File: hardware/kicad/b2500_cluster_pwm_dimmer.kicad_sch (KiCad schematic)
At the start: 35 parts, among them J1 Phoenix MKDS-1,5-5-5.08, Q1 FQP27P06, Q2 2N7000, SW1 CAL, U1 XIAO RP2040, U2 Pololu D36V28F5

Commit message: Add KiCad PCB layout (placed + poured, signal nets for GUI routing)
Generate b2500_cluster_pwm_dimmer.kicad_pcb via hardware/scripts/gen_pcb.py
(pcbnew API). Per the chosen workflow, the board is delivered placed and
ground-poured with the high-current connector nets pre-routed; the remaining
signal nets are left as ratsnest for interactive routing in the KiCad GUI.

- Signal-flow floorplan on a 94x62 mm 2-layer board, fitted against real
  footprint courtyards: connector left, input protection across the top,
  buck + 5V path top-right, DIM sense divider mid-board (kept away from the
  MOSFET switching node), MCU centre, gate drive + Q1 bottom-left by the
  output pin. Zero courtyard/edge violations.
- GND pours on both layers + stitching vias; M3 mounting holes tied to GND.
- VIN_RAW (on B.Cu) and PWM_OUT pre-routed wide with hand-authored,
  pad-avoiding waypoints. DRC clean except the deliberate signal ratsnest.
- Per-pin connector silk, USB power warning, cluster-illumination-only note,
  and all seven required test points.
- Refactor the netlist into hardware/scripts/netlist.py as the single source
  of truth shared by the schematic and board generators. Q2 -> wider-pitch
  TO-92 footprint for hand soldering and clearance.
- Top-view render committed for reference (hardware/kicad/pcb_top.png).

Co-Authored-By: Claude Fable 5 <noreply@anthropic.com>
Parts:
- Q2: footprint Package_TO_SOT_THT:TO-92_Inline -> Package_TO_SOT_THT:TO-92_Inline_Wide
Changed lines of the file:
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@@
     (property "Reference" "Q2" (at 76.2 217.14 0) (effects (font (size 1.27 1.27))))
     (property "Value" "2N7000" (at 76.2 245.14 0) (effects (font (size 1.27 1.27))))
-    (property "Footprint" "Package_TO_SOT_THT:TO-92_Inline" (at 76.2 231.14 0) (effects (font (size 1.27 1.27)) hide))
+    (property "Footprint" "Package_TO_SOT_THT:TO-92_Inline_Wide" (at 76.2 231.14 0) (effects (font (size 1.27 1.27)) hide))
     (property "Datasheet" "" (at 76.2 231.14 0) (effects (font (size 1.27 1.27)) hide))
     (property "Description" "" (at 76.2 231.14 0) (effects (font (size 1.27 1.27)) hide))

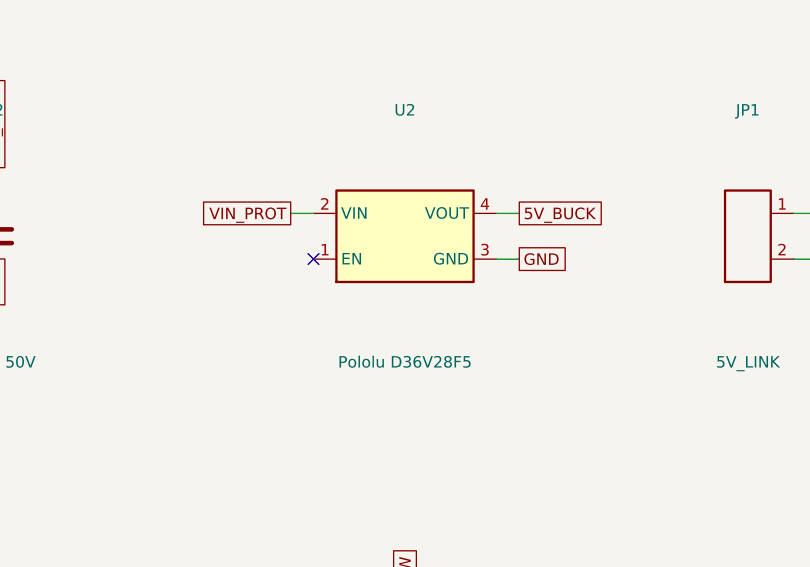
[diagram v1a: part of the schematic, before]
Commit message: Fix U2 buck land: off-board 3-pin wired header (audit finding)
A datasheet/footprint audit found the U2 land was wrong: the custom Pololu
D36V28F5 footprint had 4 pads in an unverified order, but the real module has
6 connections (offset PG plus two GNDs) and Pololu does not publish the edge
pin order in text. A mis-built buck could put 12 V on the 5 V rail.

Replace it with an orientation-proof connection: U2 is now a labeled 3-pin
header (VIN / GND / VOUT 5V) for the module mounted off-board and wired
label-to-label. EN (default-on) and PG are unused.

- netlist.py: U2 -> PinHeader_1x03, pads VIN/GND/VOUT -> VIN_PROT/GND/5V_BUCK.
- gen_sch.py: buck symbol reduced to 3 pins (VIN/GND/VOUT). ERC clean.
- gen_pcb.py: re-place U2, add per-pin silk and OFF-BOARD BUCK label, fix the
  VIN_PROT and 5V_BUCK routing pad refs. Fully routed, DRC 0/0.
- Delete the incorrect Pololu_D36V28F5.kicad_mod; refresh gerbers, BOM, docs.

Audit also verified (correct, no change): XIAO RP2040 footprint pinout plus
0.6in/0.1in spacing, FQP27P06 G-D-S, 2N7000 S-G-D, BAT54S pin-3 common, and
diode (cathode = pad 1) polarities.

Co-Authored-By: Claude Fable 5 <noreply@anthropic.com>
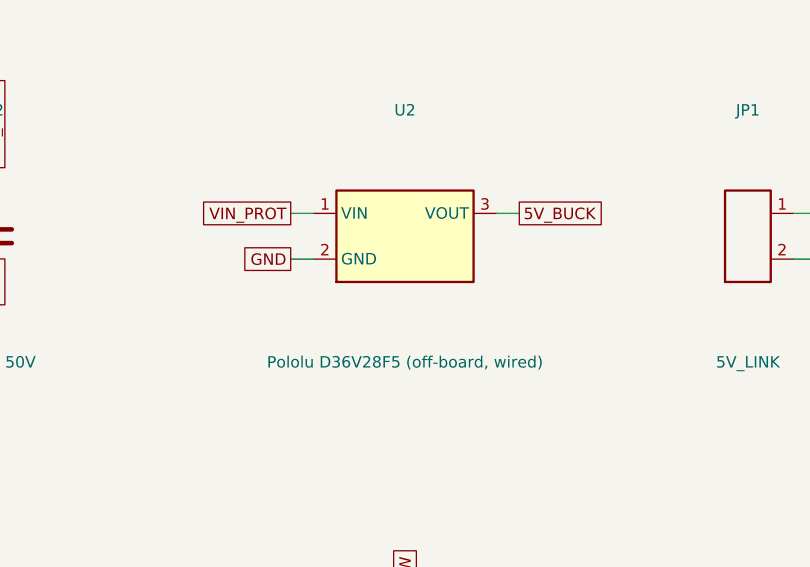
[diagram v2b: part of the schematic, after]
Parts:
- U2: value Pololu D36V28F5 -> Pololu D36V28F5 (off-board, wired); footprint b2500:Pololu_D36V28F5 -> Connector_PinHeader_2.54mm:PinHeader_1x03_P2.54mm_Vertical
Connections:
- net 5V_BUCK: now also U2.3 (VOUT); no longer U2.4 (VOUT)
- net GND: now also U2.2 (GND); no longer U2.3 (GND)
- net VIN_PROT: now also U2.1 (VIN); no longer U2.2 (VIN)
- no-connect marks 8 -> 7
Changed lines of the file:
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@@
     (exclude_from_sim no) (in_bom yes) (on_board yes) (dnp no)
     (property "Reference" "U2" (at 210.82 36.8 0) (effects (font (size 1.27 1.27))))
-    (property "Value" "Pololu D36V28F5" (at 210.82 64.8 0) (effects (font (size 1.27 1.27))))
-    (property "Footprint" "b2500:Pololu_D36V28F5" (at 210.82 50.8 0) (effects (font (size 1.27 1.27)) hide))
+    (property "Value" "Pololu D36V28F5 (off-board, wired)" (at 210.82 64.8 0) (effects (font (size 1.27 1.27))))
+    (property "Footprint" "Connector_PinHeader_2.54mm:PinHeader_1x03_P2.54mm_Vertical" (at 210.82 50.8 0) (effects (font (size 1.27 1.27)) hide))
     (property "Datasheet" "" (at 210.82 50.8 0) (effects (font (size 1.27 1.27)) hide))
     (property "Description" "" (at 210.82 50.8 0) (effects (font (size 1.27 1.27)) hide))
@@
     (pin "2")
     (pin "3")
-    (pin "4")
     (instances (project "b2500_cluster_pwm_dimmer" (path "/1ee15cb9-a36e-5ec0-9fe9-e38d32bfd5d1" (reference "U2") (unit 1))))
   )
-  (no_connect (at 200.66 53.34))
   (wire (pts (xy 200.66 48.26) (xy 198.12 48.26)) (stroke (width 0) (type default)))
   (global_label "VIN_PROT" (shape passive) (at 198.12 48.26 180) (fields_autoplaced yes) (effects (font (size 1.27 1.27)) (justify right)) (property "Intersheetrefs" "${INTERSHEET_REFS}" (at 198.12 48.26 0) (effects (font (size 1.27 1.27)) hide)))
-  (wire (pts (xy 220.98 53.34) (xy 223.52 53.34)) (stroke (width 0) (type default)))
-  (global_label "GND" (shape passive) (at 223.52 53.34 0) (fields_autoplaced yes) (effects (font (size 1.27 1.27)) (justify left)) (property "Intersheetrefs" "${INTERSHEET_REFS}" (at 223.52 53.34 0) (effects (font (size 1.27 1.27)) hide)))
+  (wire (pts (xy 200.66 53.34) (xy 198.12 53.34)) (stroke (width 0) (type default)))
+  (global_label "GND" (shape passive) (at 198.12 53.34 180) (fields_autoplaced yes) (effects (font (size 1.27 1.27)) (justify right)) (property "Intersheetrefs" "${INTERSHEET_REFS}" (at 198.12 53.34 0) (effects (font (size 1.27 1.27)) hide)))
   (wire (pts (xy 220.98 48.26) (xy 223.52 48.26)) (stroke (width 0) (type default)))
   (global_label "5V_BUCK" (shape passive) (at 223.52 48.26 0) (fields_autoplaced yes) (effects (font (size 1.27 1.27)) (justify left)) (property "Intersheetrefs" "${INTERSHEET_REFS}" (at 223.52 48.26 0) (effects (font (size 1.27 1.27)) hide)))

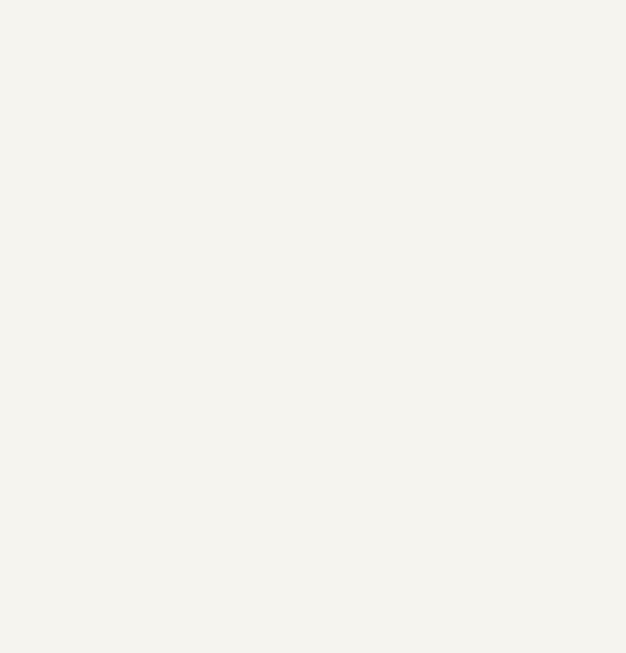
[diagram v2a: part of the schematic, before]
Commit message: Add green power-on LED (D6 + R11) on protected 12V input
Lights whenever the board has power. 3mm THT green LED with a 3.3k
series resistor (~3 mA) off VIN_PROT, placed top-right with a PWR silk
label. Schematic gains an LED symbol; fully routed, DRC 0/0; gerbers,
BOM, schematic PDF, and render refreshed.

Co-Authored-By: Claude Opus 4.8 <noreply@anthropic.com>
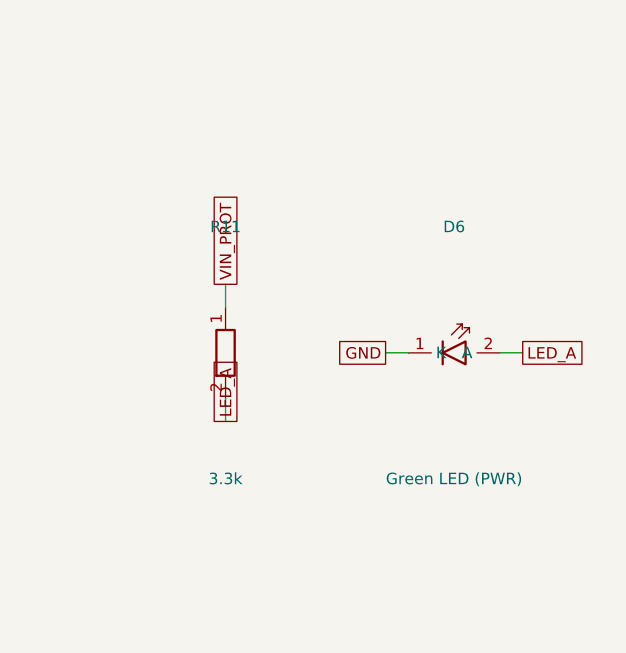
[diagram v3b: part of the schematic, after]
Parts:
- added D6: Green LED (PWR), LED_THT:LED_D3.0mm, symbol b2500:LED
- added R11: 3.3k, Resistor_SMD:R_0805_2012Metric_Pad1.20x1.40mm_HandSolder, symbol b2500:R
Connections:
- net GND: now also D6.1 (K)
- net VIN_PROT: now also R11.1
- new net LED_A: D6.2 (A), R11.2
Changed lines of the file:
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@@
   (wire (pts (xy 325.12 233.68) (xy 325.12 236.22)) (stroke (width 0) (type default)))
   (global_label "GND" (shape passive) (at 325.12 236.22 270) (fields_autoplaced yes) (effects (font (size 1.27 1.27)) (justify left)) (property "Intersheetrefs" "${INTERSHEET_REFS}" (at 325.12 236.22 0) (effects (font (size 1.27 1.27)) hide)))
+  (symbol (lib_id "b2500:R") (at 299.72 170.18 0) (unit 1)
+    (exclude_from_sim no) (in_bom yes) (on_board yes) (dnp no)
+    (property "Reference" "R11" (at 299.72 156.18 0) (effects (font (size 1.27 1.27))))
+    (property "Value" "3.3k" (at 299.72 184.18 0) (effects (font (size 1.27 1.27))))
+    (property "Footprint" "Resistor_SMD:R_0805_2012Metric_Pad1.20x1.40mm_HandSolder" (at 299.72 170.18 0) (effects (font (size 1.27 1.27)) hide))
+    (property "Datasheet" "" (at 299.72 170.18 0) (effects (font (size 1.27 1.27)) hide))
+    (property "Description" "" (at 299.72 170.18 0) (effects (font (size 1.27 1.27)) hide))
+    (pin "1")
+    (pin "2")
+    (instances (project "b2500_cluster_pwm_dimmer" (path "/1ee15cb9-a36e-5ec0-9fe9-e38d32bfd5d1" (reference "R11") (unit 1))))
+  )
+  (wire (pts (xy 299.72 165.1) (xy 299.72 162.56)) (stroke (width 0) (type default)))
+  (global_label "VIN_PROT" (shape passive) (at 299.72 162.56 90) (fields_autoplaced yes) (effects (font (size 1.27 1.27)) (justify left)) (property "Intersheetrefs" "${INTERSHEET_REFS}" (at 299.72 162.56 0) (effects (font (size 1.27 1.27)) hide)))
+  (wire (pts (xy 299.72 175.26) (xy 299.72 177.8)) (stroke (width 0) (type default)))
+  (global_label "LED_A" (shape passive) (at 299.72 177.8 270) (fields_autoplaced yes) (effects (font (size 1.27 1.27)) (justify left)) (property "Intersheetrefs" "${INTERSHEET_REFS}" (at 299.72 177.8 0) (effects (font (size 1.27 1.27)) hide)))
+  (symbol (lib_id "b2500:LED") (at 325.12 170.18 0) (unit 1)
+    (exclude_from_sim no) (in_bom yes) (on_board yes) (dnp no)
+    (property "Reference" "D6" (at 325.12 156.18 0) (effects (font (size 1.27 1.27))))
+    (property "Value" "Green LED (PWR)" (at 325.12 184.18 0) (effects (font (size 1.27 1.27))))
+    (property "Footprint" "LED_THT:LED_D3.0mm" (at 325.12 170.18 0) (effects (font (size 1.27 1.27)) hide))
+    (property "Datasheet" "" (at 325.12 170.18 0) (effects (font (size 1.27 1.27)) hide))
+    (property "Description" "" (at 325.12 170.18 0) (effects (font (size 1.27 1.27)) hide))
+    (pin "1")
+    (pin "2")
+    (instances (project "b2500_cluster_pwm_dimmer" (path "/1ee15cb9-a36e-5ec0-9fe9-e38d32bfd5d1" (reference "D6") (unit 1))))
+  )
+  (wire (pts (xy 320.04 170.18) (xy 317.5 170.18)) (stroke (width 0) (type default)))
+  (global_label "GND" (shape passive) (at 317.5 170.18 180) (fields_autoplaced yes) (effects (font (size 1.27 1.27)) (justify right)) (property "Intersheetrefs" "${INTERSHEET_REFS}" (at 317.5 170.18 0) (effects (font (size 1.27 1.27)) hide)))
+  (wire (pts (xy 330.2 170.18) (xy 332.74 170.18)) (stroke (width 0) (type default)))
+  (global_label "LED_A" (shape passive) (at 332.74 170.18 0) (fields_autoplaced yes) (effects (font (size 1.27 1.27)) (justify left)) (property "Intersheetrefs" "${INTERSHEET_REFS}" (at 332.74 170.18 0) (effects (font (size 1.27 1.27)) hide)))
   (text "Power input: fused 12V lights feed -> reverse protection -> TVS -> bulk caps -> buck + high-side switch" (exclude_from_sim no) (at 40 30 0) (effects (font (size 1.27 1.27))))
   (text "DIM sense: factory rheostat output, high-impedance divider 100k/22k, RC filter, BAT54S clamp" (exclude_from_sim no) (at 40 90 0) (effects (font (size 1.27 1.27))))
